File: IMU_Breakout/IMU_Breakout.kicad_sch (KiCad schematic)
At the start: 6 parts, among them J1 IMU_Connector, U1 LSM6DSL

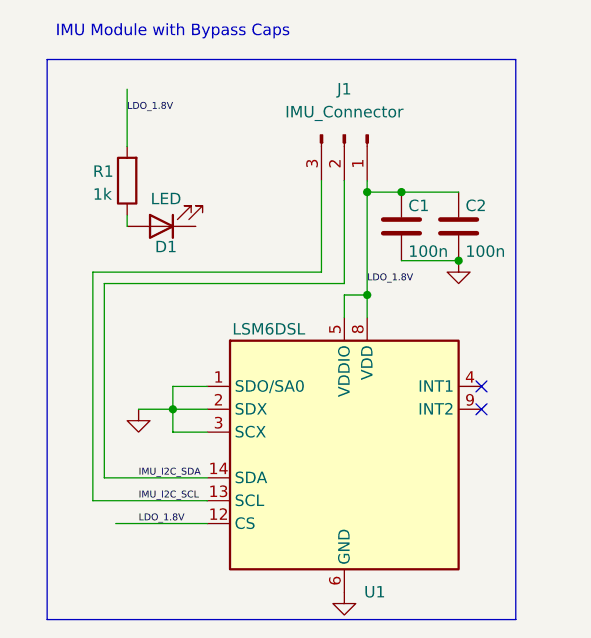
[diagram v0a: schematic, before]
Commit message: Made Mag compact
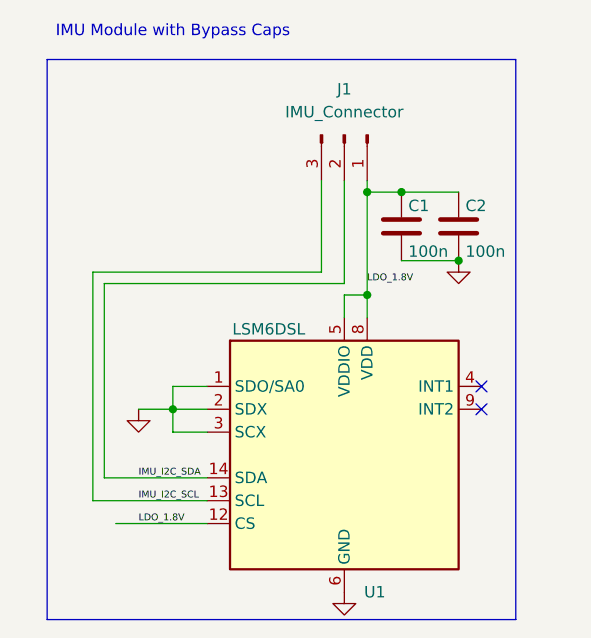
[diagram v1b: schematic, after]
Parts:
- removed D1: LED, symbol Device:LED
- removed R1: 1k, symbol Device:R
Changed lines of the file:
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@@
-	(wire
-		(pts
-			(xy 123.19 107.95) (xy 123.19 109.22)
-		)
-		(stroke
-			(width 0)
-			(type default)
-		)
-	)
 	(wire
 		(pts
@@
 	(wire
 		(pts
-			(xy 123.19 93.98) (xy 123.19 100.33)
-		)
-		(stroke
-			(width 0)
-			(type default)
-		)
-	)
-	(wire
-		(pts
 			(xy 132.08 127) (xy 128.27 127)
 		)
@@
 				(size 1.27 1.27)
 			)
-		)
-	)
-	(label "LDO_1.8V"
-		(at 123.19 96.52 0)
-		(fields_autoplaced yes)
-		(effects
-			(font
-				(size 0.762 0.762)
-			)
-			(justify left bottom)
 		)
 	)
@@
 		)
 	)
-	(symbol
-		(lib_id "Device:R")
-		(at 123.19 104.14 180)
-		(unit 1)
-		(exclude_from_sim no)
-		(in_bom yes)
-		(on_board yes)
-		(dnp no)
-		(property "Reference" "R1"
-			(at 119.38 103.124 0)
-			(effects
-				(font
-					(size 1.27 1.27)
-				)
-				(justify right)
-			)
-		)
-		(property "Value" "1k"
-			(at 119.38 105.664 0)
-			(effects
-				(font
-					(size 1.27 1.27)
-				)
-				(justify right)
-			)
-		)
-		(property "Footprint" ""
-			(at 124.968 104.14 90)
-			(effects
-				(font
-					(size 1.27 1.27)
-				)
-				(hide yes)
-			)
-		)
-		(property "Datasheet" "~"
-			(at 123.19 104.14 0)
-			(effects
-				(font
-					(size 1.27 1.27)
-				)
-				(hide yes)
-			)
-		)
-		(property "Description" "Resistor"
-			(at 123.19 104.14 0)
-			(effects
-				(font
-					(size 1.27 1.27)
-				)
-				(hide yes)
-			)
-		)
-		(pin "1"
-		)
-		(pin "2"
-		)
-		(instances
-			(project ""
-				(path "/3b407343-5ff9-4b26-8d91-ce71bebfc022"
-					(reference "R1")
-					(unit 1)
-				)
-			)
-		)
-	)
-	(symbol
-		(lib_id "Device:LED")
-		(at 127 109.22 180)
-		(unit 1)
-		(exclude_from_sim no)
-		(in_bom yes)
-		(on_board yes)
-		(dnp no)
-		(property "Reference" "D1"
-			(at 127.508 111.506 0)
-			(effects
-				(font
-					(size 1.27 1.27)
-				)
-			)
-		)
-		(property "Value" "LED"
-			(at 127.508 106.172 0)
-			(effects
-				(font
-					(size 1.27 1.27)
-				)
-			)
-		)
-		(property "Footprint" ""
-			(at 127 109.22 0)
-			(effects
-				(font
-					(size 1.27 1.27)
-				)
-				(hide yes)
-			)
-		)
-		(property "Datasheet" "~"
-			(at 127 109.22 0)
-			(effects
-				(font
-					(size 1.27 1.27)
-				)
-				(hide yes)
-			)
-		)
-		(property "Description" "Light emitting diode"
-			(at 127 109.22 0)
-			(effects
-				(font
-					(size 1.27 1.27)
-				)
-				(hide yes)
-			)
-		)
-		(pin "1"
-		)
-		(pin "2"
-		)
-		(instances
-			(project ""
-				(path "/3b407343-5ff9-4b26-8d91-ce71bebfc022"
-					(reference "D1")
-					(unit 1)
-				)
-			)
-		)
-	)

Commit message: Switched connectors
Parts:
- J1: footprint Connector_Molex:Molex_Nano-Fit_105313-xx03_1x03_P2.50mm_Horizontal -> UTSVT_Connectors:Molex_MicroFit3.0_1x3xP3.00mm_PolarizingPeg_Vertical
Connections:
- net IMU_I2C_SCL: now also J1.2 (Pin_2); no longer J1.3 (Pin_3)
- net IMU_I2C_SDA: now also J1.3 (Pin_3); no longer J1.2 (Pin_2)
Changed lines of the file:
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@@
-	(wire
-		(pts
-			(xy 144.78 114.3) (xy 119.38 114.3)
-		)
-		(stroke
-			(width 0)
-			(type default)
-		)
-	)
 	(wire
 		(pts
@@
 	(wire
 		(pts
-			(xy 147.32 115.57) (xy 120.65 115.57)
-		)
-		(stroke
-			(width 0)
-			(type default)
-		)
-	)
-	(wire
-		(pts
-			(xy 119.38 114.3) (xy 119.38 139.7)
-		)
-		(stroke
-			(width 0)
-			(type default)
-		)
-	)
-	(wire
-		(pts
 			(xy 128.27 129.54) (xy 132.08 129.54)
 		)
@@
 		(pts
 			(xy 132.08 132.08) (xy 128.27 132.08)
-		)
-		(stroke
-			(width 0)
-			(type default)
-		)
-	)
-	(wire
-		(pts
-			(xy 120.65 115.57) (xy 120.65 137.16)
 		)
 		(stroke
@@
 	(label "LDO_1.8V"
 		(at 124.46 142.24 0)
+		(fields_autoplaced yes)
+		(effects
+			(font
+				(size 0.762 0.762)
+			)
+			(justify left bottom)
+		)
+	)
+	(label "IMU_I2C_SDA"
+		(at 144.78 111.76 90)
+		(fields_autoplaced yes)
+		(effects
+			(font
+				(size 0.762 0.762)
+			)
+			(justify left bottom)
+		)
+	)
+	(label "IMU_I2C_SCL"
+		(at 147.32 111.76 90)
 		(fields_autoplaced yes)
 		(effects
@@
 			)
 		)
-		(property "Footprint" "Connector_Molex:Molex_Nano-Fit_105313-xx03_1x03_P2.50mm_Horizontal"
+		(property "Footprint" "UTSVT_Connectors:Molex_MicroFit3.0_1x3xP3.00mm_PolarizingPeg_Vertical"
 			(at 147.32 99.06 0)
 			(effects

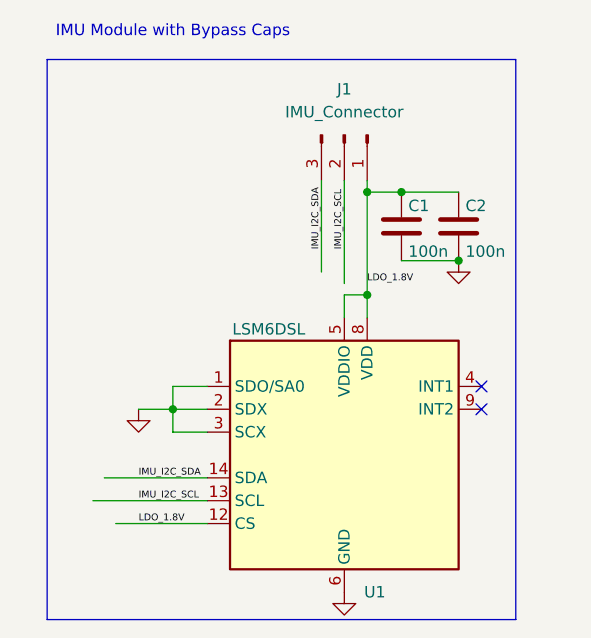
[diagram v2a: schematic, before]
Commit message: Approved Connectors and gnd connected
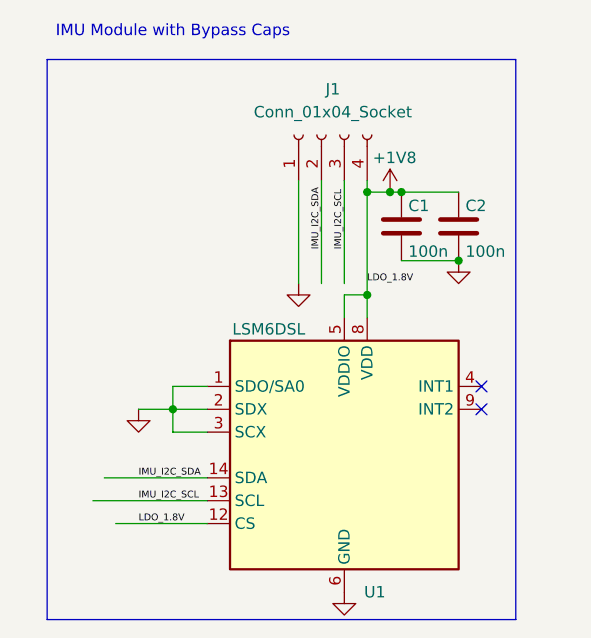
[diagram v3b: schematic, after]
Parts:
- removed J1: IMU_Connector, UTSVT_Connectors:Molex_MicroFit3.0_1x3xP3.00mm_PolarizingPeg_Vertical, symbol Connector:Conn_01x03_Pin
- added J1: Conn_01x04_Socket, Connector_Molex:Molex_Nano-Fit_105309-xx04_1x04_P2.50mm_Vertical, symbol Connector:Conn_01x04_Socket
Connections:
- net GND: now also J1.1 (Pin_1)
- net IMU_I2C_SCL: now also J1.3 (Pin_3)
- net IMU_I2C_SDA: now also J1.2 (Pin_2)
- net LDO_1.8V renamed +1V8
- net +1V8: now also J1.4 (Pin_4)
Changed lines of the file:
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@@
+		(color 0 0 0 0)
+	)
+	(junction
+		(at 152.4 105.41)
+		(diameter 0)
 		(color 0 0 0 0)
 	)
@@
 	(wire
 		(pts
-			(xy 149.86 105.41) (xy 153.67 105.41)
+			(xy 149.86 105.41) (xy 152.4 105.41)
 		)
 		(stroke
@@
 	(wire
 		(pts
+			(xy 142.24 104.14) (xy 142.24 115.57)
+		)
+		(stroke
+			(width 0)
+			(type default)
+		)
+	)
+	(wire
+		(pts
 			(xy 149.86 116.84) (xy 147.32 116.84)
 		)
@@
 	(wire
 		(pts
-			(xy 144.78 104.14) (xy 144.78 114.3)
+			(xy 152.4 105.41) (xy 153.67 105.41)
+		)
+		(stroke
+			(width 0)
+			(type default)
+		)
+	)
+	(wire
+		(pts
+			(xy 144.78 104.14) (xy 144.78 115.57)
 		)
 		(stroke
@@
 	)
 	(symbol
+		(lib_id "Connector:Conn_01x04_Socket")
+		(at 144.78 99.06 90)
+		(unit 1)
+		(exclude_from_sim no)
+		(in_bom yes)
+		(on_board yes)
+		(dnp no)
+		(fields_autoplaced yes)
+		(property "Reference" "J1"
+			(at 146.05 93.98 90)
+			(effects
+				(font
+					(size 1.27 1.27)
+				)
+			)
+		)
+		(property "Value" "Conn_01x04_Socket"
+			(at 146.05 96.52 90)
+			(effects
+				(font
+					(size 1.27 1.27)
+				)
+			)
+		)
+		(property "Footprint" "Connector_Molex:Molex_Nano-Fit_105309-xx04_1x04_P2.50mm_Vertical"
+			(at 144.78 99.06 0)
+			(effects
+				(font
+					(size 1.27 1.27)
+				)
+				(hide yes)
+			)
+		)
+		(property "Datasheet" "~"
+			(at 144.78 99.06 0)
+			(effects
+				(font
+					(size 1.27 1.27)
+				)
+				(hide yes)
+			)
+		)
+		(property "Description" "Generic connector, single row, 01x04, script generated"
+			(at 144.78 99.06 0)
+			(effects
+				(font
+					(size 1.27 1.27)
+				)
+				(hide yes)
+			)
+		)
+		(pin "4"
+		)
+		(pin "1"
+		)
+		(pin "2"
+		)
+		(pin "3"
+		)
+		(instances
+			(project ""
+				(path "/3b407343-5ff9-4b26-8d91-ce71bebfc022"
+					(reference "J1")
+					(unit 1)
+				)
+			)
+		)
+	)
+	(symbol
 		(lib_id "Device:C")
 		(at 153.67 109.22 0)
@@
 	)
 	(symbol
-		(lib_id "Connector:Conn_01x03_Pin")
-		(at 147.32 99.06 270)
+		(lib_id "power:+1V8")
+		(at 152.4 105.41 0)
 		(unit 1)
 		(exclude_from_sim no)
@@
 		(on_board yes)
 		(dnp no)
-		(fields_autoplaced yes)
-		(property "Reference" "J1"
-			(at 147.32 93.98 90)
-			(effects
-				(font
-					(size 1.27 1.27)
-				)
-			)
-		)
-		(property "Value" "IMU_Connector"
-			(at 147.32 96.52 90)
-			(effects
-				(font
-					(size 1.27 1.27)
-				)
-			)
-		)
-		(property "Footprint" "UTSVT_Connectors:Molex_MicroFit3.0_1x3xP3.00mm_PolarizingPeg_Vertical"
-			(at 147.32 99.06 0)
-			(effects
-				(font
-					(size 1.27 1.27)
-				)
-				(hide yes)
-			)
-		)
-		(property "Datasheet" "~"
-			(at 147.32 99.06 0)
-			(effects
-				(font
-					(size 1.27 1.27)
-				)
-				(hide yes)
-			)
-		)
-		(property "Description" "Generic connector, single row, 01x03, script generated"
-			(at 147.32 99.06 0)
-			(effects
-				(font
-					(size 1.27 1.27)
-				)
-				(hide yes)
-			)
-		)
-		(pin "3"
+		(property "Reference" "#PWR04"
+			(at 152.4 109.22 0)
+			(effects
+				(font
+					(size 1.27 1.27)
+				)
+				(hide yes)
+			)
+		)
+		(property "Value" "+1V8"
+			(at 152.908 101.6 0)
+			(effects
+				(font
+					(size 1.27 1.27)
+				)
+			)
+		)
+		(property "Footprint" ""
+			(at 152.4 105.41 0)
+			(effects
+				(font
+					(size 1.27 1.27)
+				)
+				(hide yes)
+			)
+		)
+		(property "Datasheet" ""
+			(at 152.4 105.41 0)
+			(effects
+				(font
+					(size 1.27 1.27)
+				)
+				(hide yes)
+			)
+		)
+		(property "Description" "Power symbol creates a global label with name \"+1V8\""
+			(at 152.4 105.41 0)
+			(effects
+				(font
+					(size 1.27 1.27)
+				)
+				(hide yes)
+			)
 		)
 		(pin "1"
-		)
-		(pin "2"
 		)
 		(instances
 			(project ""
 				(path "/3b407343-5ff9-4b26-8d91-ce71bebfc022"
-					(reference "J1")
+					(reference "#PWR04")
 					(unit 1)
 				)
@@
 					(unit 1)
 				)
+			)
+		)
+	)
+	(symbol
+		(lib_id "power:GND")
+		(at 142.24 115.57 0)
+		(unit 1)
+		(exclude_from_sim no)
+		(in_bom yes)
+		(on_board yes)
+		(dnp no)
+		(fields_autoplaced yes)
+		(property "Reference" "#PWR05"
+			(at 142.24 121.92 0)
+			(effects
+				(font
+					(size 1.27 1.27)
+				)
+				(hide yes)
+			)
+		)
+		(property "Value" "GND"
+			(at 142.24 120.65 0)
+			(effects
+				(font
+					(size 1.27 1.27)
+				)
+				(hide yes)
+			)
+		)
+		(property "Footprint" ""
+			(at 142.24 115.57 0)
+			(effects
+				(font
+					(size 1.27 1.27)
+				)
+				(hide yes)
+			)
+		)
+		(property "Datasheet" ""
+			(at 142.24 115.57 0)
+			(effects
+				(font
+					(size 1.27 1.27)
+				)
+				(hide yes)
+			)
+		)
+		(property "Description" "Power symbol creates a global label with name \"GND\" , ground"
+			(at 142.24 115.57 0)
+			(effects
+				(font
+					(size 1.27 1.27)
+				)
+				(hide yes)
+			)
+		)
+		(pin "1"
+		)
+		(instances
+			(project ""
+				(path "/3b407343-5ff9-4b26-8d91-ce71bebfc022"
+					(reference "#PWR05")
+					(unit 1)
+				)

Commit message: fixed review stuffs
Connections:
- net +1V8 renamed +3V3
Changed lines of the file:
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@@
 		)
 	)
-	(label "LDO_1.8V"
+	(label "3.3V"
 		(at 124.46 142.24 0)
 		(fields_autoplaced yes)
@@
 		)
 	)
-	(label "LDO_1.8V"
+	(label "3.3V"
 		(at 149.86 115.57 0)
 		(fields_autoplaced yes)
@@
 			)
 		)
-		(property "Value" "+1V8"
+		(property "Value" "+3V3"
 			(at 152.908 101.6 0)
 			(effects

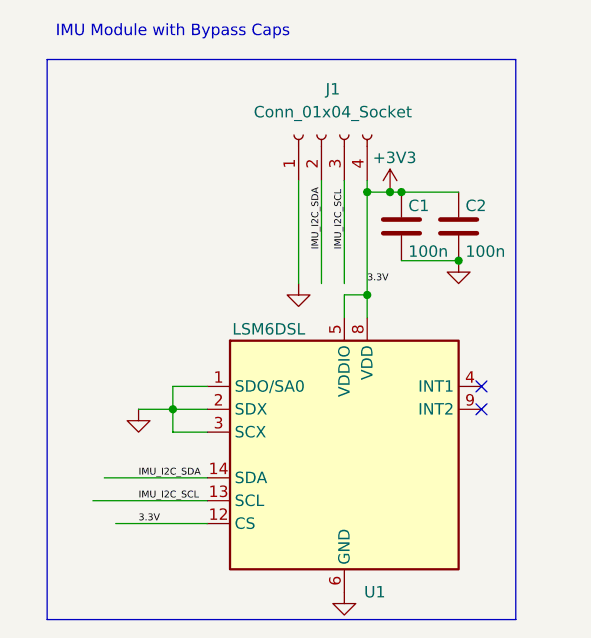
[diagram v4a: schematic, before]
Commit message: fixed imu connector oops
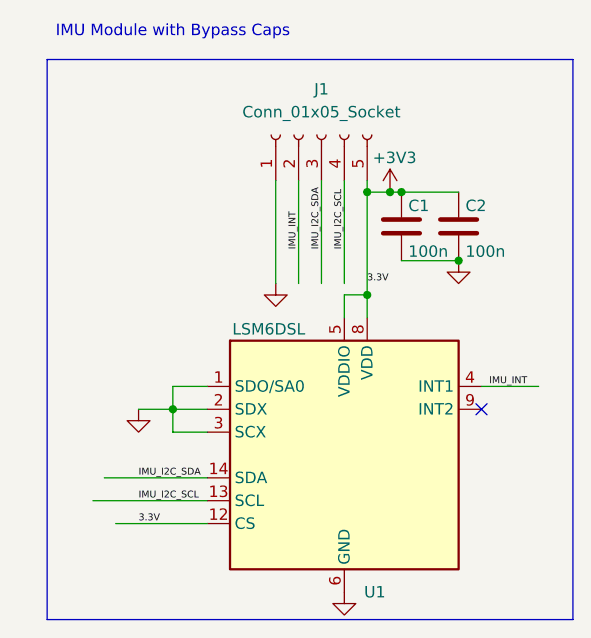
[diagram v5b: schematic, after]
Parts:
- removed J1: Conn_01x04_Socket, Connector_Molex:Molex_Nano-Fit_105309-xx04_1x04_P2.50mm_Vertical, symbol Connector:Conn_01x04_Socket
- added J1: Conn_01x05_Socket, Connector_Molex:Molex_Nano-Fit_105309-xx05_1x05_P2.50mm_Vertical, symbol Connector:Conn_01x05_Socket
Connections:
- net +3V3: now also J1.5 (Pin_5)
- net GND: now also J1.1 (Pin_1)
- net IMU_I2C_SCL: now also J1.4 (Pin_4)
- net IMU_I2C_SDA: now also J1.3 (Pin_3)
- net IMU_INT: now reaches U1.4 (INT1)
- net IMU_INT: now also J1.2 (Pin_2)
- no-connect marks 2 -> 1
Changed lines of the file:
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@@
-	)
-	(no_connect
-		(at 162.56 127)
 	)
 	(no_connect
@@
 	(wire
 		(pts
+			(xy 142.24 104.14) (xy 142.24 115.57)
+		)
+		(stroke
+			(width 0)
+			(type default)
+		)
+	)
+	(wire
+		(pts
 			(xy 124.46 129.54) (xy 128.27 129.54)
 		)
@@
 	(wire
 		(pts
-			(xy 142.24 104.14) (xy 142.24 115.57)
+			(xy 139.7 104.14) (xy 139.7 115.57)
 		)
 		(stroke
@@
 		(pts
 			(xy 144.78 104.14) (xy 144.78 115.57)
+		)
+		(stroke
+			(width 0)
+			(type default)
+		)
+	)
+	(wire
+		(pts
+			(xy 162.56 127) (xy 168.91 127)
 		)
 		(stroke
@@
 	(rectangle
 		(start 114.3 90.678)
-		(end 166.37 152.908)
+		(end 172.72 152.908)
 		(stroke
 			(width 0)
@@
 		)
 	)
-	(label "3.3V"
-		(at 124.46 142.24 0)
+	(label "IMU_INT"
+		(at 167.64 127 180)
 		(fields_autoplaced yes)
 		(effects
@@
 				(size 0.762 0.762)
 			)
-			(justify left bottom)
-		)
-	)
-	(label "IMU_I2C_SDA"
-		(at 144.78 111.76 90)
+			(justify right bottom)
+		)
+	)
+	(label "3.3V"
+		(at 124.46 142.24 0)
 		(fields_autoplaced yes)
 		(effects
@@
 		)
 	)
-	(label "IMU_I2C_SCL"
-		(at 147.32 111.76 90)
+	(label "IMU_I2C_SDA"
+		(at 144.78 111.76 90)
 		(fields_autoplaced yes)
 		(effects
@@
 		)
 	)
-	(label "3.3V"
-		(at 149.86 115.57 0)
+	(label "IMU_I2C_SCL"
+		(at 147.32 111.76 90)
 		(fields_autoplaced yes)
 		(effects
@@
 		)
 	)
-	(label "IMU_I2C_SCL"
-		(at 124.46 139.7 0)
+	(label "3.3V"
+		(at 149.86 115.57 0)
 		(fields_autoplaced yes)
 		(effects
@@
 		)
 	)
-	(label "IMU_I2C_SDA"
-		(at 124.46 137.16 0)
+	(label "IMU_I2C_SCL"
+		(at 124.46 139.7 0)
 		(fields_autoplaced yes)
 		(effects
@@
 			)
 			(justify left bottom)
+		)
+	)
+	(label "IMU_INT"
+		(at 142.24 111.76 90)
+		(fields_autoplaced yes)
+		(effects
+			(font
+				(size 0.762 0.762)
+			)
+			(justify left bottom)
+		)
+	)
+	(label "IMU_I2C_SDA"
+		(at 124.46 137.16 0)
+		(fields_autoplaced yes)
+		(effects
+			(font
+				(size 0.762 0.762)
+			)
+			(justify left bottom)
+		)
+	)
+	(symbol
+		(lib_id "Connector:Conn_01x05_Socket")
+		(at 144.78 99.06 90)
+		(unit 1)
+		(exclude_from_sim no)
+		(in_bom yes)
+		(on_board yes)
+		(dnp no)
+		(fields_autoplaced yes)
+		(property "Reference" "J1"
+			(at 144.78 93.98 90)
+			(effects
+				(font
+					(size 1.27 1.27)
+				)
+			)
+		)
+		(property "Value" "Conn_01x05_Socket"
+			(at 144.78 96.52 90)
+			(effects
+				(font
+					(size 1.27 1.27)
+				)
+			)
+		)
+		(property "Footprint" "Connector_Molex:Molex_Nano-Fit_105309-xx05_1x05_P2.50mm_Vertical"
+			(at 144.78 99.06 0)
+			(effects
+				(font
+					(size 1.27 1.27)
+				)
+				(hide yes)
+			)
+		)
+		(property "Datasheet" "~"
+			(at 144.78 99.06 0)
+			(effects
+				(font
+					(size 1.27 1.27)
+				)
+				(hide yes)
+			)
+		)
+		(property "Description" "Generic connector, single row, 01x05, script generated"
+			(at 144.78 99.06 0)
+			(effects
+				(font
+					(size 1.27 1.27)
+				)
+				(hide yes)
+			)
+		)
+		(pin "3"
+		)
+		(pin "4"
+		)
+		(pin "5"
+		)
+		(pin "2"
+		)
+		(pin "1"
+		)
+		(instances
+			(project "IMU_Breakout"
+				(path "/3b407343-5ff9-4b26-8d91-ce71bebfc022"
+					(reference "J1")
+					(unit 1)
+				)
+			)
 		)
 	)
@@
 	)
 	(symbol
-		(lib_id "Connector:Conn_01x04_Socket")
-		(at 144.78 99.06 90)
-		(unit 1)
-		(exclude_from_sim no)
-		(in_bom yes)
-		(on_board yes)
-		(dnp no)
-		(fields_autoplaced yes)
-		(property "Reference" "J1"
-			(at 146.05 93.98 90)
-			(effects
-				(font
-					(size 1.27 1.27)
-				)
-			)
-		)
-		(property "Value" "Conn_01x04_Socket"
-			(at 146.05 96.52 90)
-			(effects
-				(font
-					(size 1.27 1.27)
-				)
-			)
-		)
-		(property "Footprint" "Connector_Molex:Molex_Nano-Fit_105309-xx04_1x04_P2.50mm_Vertical"
-			(at 144.78 99.06 0)
-			(effects
-				(font
-					(size 1.27 1.27)
-				)
-				(hide yes)
-			)
-		)
-		(property "Datasheet" "~"
-			(at 144.78 99.06 0)
-			(effects
-				(font
-					(size 1.27 1.27)
-				)
-				(hide yes)
-			)
-		)
-		(property "Description" "Generic connector, single row, 01x04, script generated"
-			(at 144.78 99.06 0)
-			(effects
-				(font
-					(size 1.27 1.27)
-				)
-				(hide yes)
-			)
-		)
-		(pin "4"
-		)
-		(pin "1"
-		)
-		(pin "2"
-		)
-		(pin "3"
-		)
-		(instances
-			(project ""
-				(path "/3b407343-5ff9-4b26-8d91-ce71bebfc022"
-					(reference "J1")
-					(unit 1)
-				)
-			)
-		)
-	)
-	(symbol
 		(lib_id "Device:C")
 		(at 153.67 109.22 0)
@@
 	)
 	(symbol
+		(lib_id "power:GND")
+		(at 139.7 115.57 0)
+		(unit 1)
+		(exclude_from_sim no)
+		(in_bom yes)
+		(on_board yes)
+		(dnp no)
+		(fields_autoplaced yes)
+		(property "Reference" "#PWR05"
+			(at 139.7 121.92 0)
+			(effects
+				(font
+					(size 1.27 1.27)
+				)
+				(hide yes)
+			)
+		)
+		(property "Value" "GND"
+			(at 139.7 120.65 0)
+			(effects
+				(font
+					(size 1.27 1.27)
+				)
+				(hide yes)
+			)
+		)
+		(property "Footprint" ""
+			(at 139.7 115.57 0)
+			(effects
+				(font
+					(size 1.27 1.27)
+				)
+				(hide yes)
+			)
+		)
+		(property "Datasheet" ""
+			(at 139.7 115.57 0)
+			(effects
+				(font
+					(size 1.27 1.27)
+				)
+				(hide yes)
+			)
+		)
+		(property "Description" "Power symbol creates a global label with name \"GND\" , ground"
+			(at 139.7 115.57 0)
+			(effects
+				(font
+					(size 1.27 1.27)
+				)
+				(hide yes)
+			)
+		)
+		(pin "1"
+		)
+		(instances
+			(project "IMU_Breakout"
+				(path "/3b407343-5ff9-4b26-8d91-ce71bebfc022"
+					(reference "#PWR05")
+					(unit 1)
+				)
+			)
+		)
+	)
+	(symbol
 		(lib_id "Sensor_Motion:LSM6DSL")
 		(at 147.32 134.62 0)
@@
 					(unit 1)
 				)
-			)
-		)
-	)
-	(symbol
-		(lib_id "power:GND")
-		(at 142.24 115.57 0)
-		(unit 1)
-		(exclude_from_sim no)
-		(in_bom yes)
-		(on_board yes)
-		(dnp no)
-		(fields_autoplaced yes)
-		(property "Reference" "#PWR05"
-			(at 142.24 121.92 0)
-			(effects
-				(font
-					(size 1.27 1.27)
-				)
-				(hide yes)
-			)
-		)
-		(property "Value" "GND"
-			(at 142.24 120.65 0)
-			(effects
-				(font
-					(size 1.27 1.27)
-				)
-				(hide yes)
-			)
-		)
-		(property "Footprint" ""
-			(at 142.24 115.57 0)
-			(effects
-				(font
-					(size 1.27 1.27)
-				)
-				(hide yes)
-			)
-		)
-		(property "Datasheet" ""
-			(at 142.24 115.57 0)
-			(effects
-				(font
-					(size 1.27 1.27)
-				)
-				(hide yes)
-			)
-		)
-		(property "Description" "Power symbol creates a global label with name \"GND\" , ground"
-			(at 142.24 115.57 0)
-			(effects
-				(font
-					(size 1.27 1.27)
-				)
-				(hide yes)
-			)
-		)
-		(pin "1"
-		)
-		(instances
-			(project ""
-				(path "/3b407343-5ff9-4b26-8d91-ce71bebfc022"
-					(reference "#PWR05")
-					(unit 1)
-				)
